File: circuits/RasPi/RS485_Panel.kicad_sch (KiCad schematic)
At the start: 43 parts, among them J8 Conn_01x07_MountingPin, Q18 S8550, Q19 S8550, Q20 S8550, Q3 S8550, Q4 S8550, Q5 S8550, U10 MAX3485, U11 MAX3485, U12 MAX3485, U13 MAX3485, U8 MAX3485, U9 MAX3485

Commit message: PDFプロット
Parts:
- removed C37: 0.1uF, Capacitor_SMD:C_0402_1005Metric, symbol Device:C
- removed Q20: S8550, Package_TO_SOT_SMD:SOT-23, symbol Device:Q_PNP_BEC
- removed R88, R93, R94: 2.2k, Resistor_SMD:R_0402_1005Metric, symbol Device:R
- removed R91: 7.5k, Resistor_SMD:R_0603_1608Metric, symbol Device:R
- removed R92: 20k, Resistor_SMD:R_0402_1005Metric, symbol Device:R
- removed U13: MAX3485, Package_SO:SOP-8_3.9x4.9mm_P1.27mm, symbol Interface_UART:MAX3485
- added C14: 0.1uF, Capacitor_SMD:C_0402_1005Metric, symbol Device:C
- added Q2: S8550, Package_TO_SOT_SMD:SOT-23, symbol Device:Q_PNP_BEC
- added R24, R28: 7.5k, Resistor_SMD:R_0603_1608Metric, symbol Device:R
- added R25: 20k, Resistor_SMD:R_0402_1005Metric, symbol Device:R
- added R26, R27: 2.2k, Resistor_SMD:R_0402_1005Metric, symbol Device:R
- added U5: MAX3485, Package_SO:SOP-8_3.9x4.9mm_P1.27mm, symbol Interface_UART:MAX3485
- J8: footprint (none) -> Connector_Molex:Molex_PicoBlade_53261-0771_1x07-1MP_P1.25mm_Horizontal
- R34, R38, R74, R78: value 7.5k -> 20k; footprint Resistor_SMD:R_0603_1608Metric -> Resistor_SMD:R_0402_1005Metric
- R35, R39, R75, R79: value 20k -> 2.2k
- R37, R41, R77: value 2.2k -> 7.5k; footprint Resistor_SMD:R_0402_1005Metric -> Resistor_SMD:R_0603_1608Metric
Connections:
- net +3.3V: now also R35.1, R75.1, R79.1, C14.1, Q2.2 (E), R26.1, U5.8 (VCC); no longer C33.1, Q5.2 (E), R36.1, R40.1, R76.1, R87.1, U10.8 (VCC)
- net GNDD: now also R34.2, R36.2, R38.2, R40.2, R74.2, R76.2, R78.2, R87.2, C14.2, R25.2, R27.2, U5.5 (GND); no longer R35.2, R37.2, R39.2, R41.2, R75.2, R77.2, R79.2
- net RS485_Panel0: now also U5.6 (A)
- net at R34.1: now also Q4.3 (C), U9.2 (~{RE}), U9.3 (DE); no longer Q4.1 (B)
- net FPGARX_Panel3TX: now reaches U10.1 (RO)
- net at Q5.3 (C), U10.2 (~{RE}), U10.3 (DE): now also R38.1; no longer R39.1
- net FPGARX_Panel2TX: now reaches U9.1 (RO)
- net at Q18.3 (C): now also R74.1, U11.2 (~{RE}), U11.3 (DE)
- net at U12.7 (B): now also R79.2, R87.1; no longer R87.2
- net at Q18.1 (B): now also R41.1
- net at R78.1: now also Q19.3 (C), U12.2 (~{RE}), U12.3 (DE)
- net FPGARX_Panel5TX: now reaches U12.1 (RO)
- net at Q5.1 (B): now also R37.1; no longer R38.1
- net FPGARX_Panel4TX: now reaches U11.1 (RO)
- net at Q19.1 (B): now also R77.1; no longer R74.1
- net FPGARX_Panel1TX: now reaches U8.1 (RO)
- net Panel1 renamed FPGATX_Panel1RX
- net Panel2 renamed FPGATX_Panel2RX
- net FPGATX_Panel2RX: now also R28.2; no longer R34.2
- net Panel3 renamed FPGATX_Panel3RX
- net FPGATX_Panel3RX: now also R37.2; no longer R38.2
- net Panel4 renamed FPGATX_Panel4RX
- net FPGATX_Panel4RX: now also R41.2; no longer R74.2
- net Panel5 renamed FPGATX_Panel5RX
- net FPGATX_Panel5RX: now also R77.2; no longer R78.2
- new net: R35.2, R36.1, U9.7 (B)
- new net: Q2.1 (B), R24.1
- new net: R39.2, R40.1, U10.7 (B)
- new net: R75.2, R76.1, U11.7 (B)
- new net: C33.1, Q5.2 (E), R39.1, U10.8 (VCC)
- new net: R26.2, R27.1, U5.7 (B)
- new net: Q4.1 (B), R28.1
- new net: Q2.3 (C), R25.1, U5.2 (~{RE}), U5.3 (DE)
- new net FPGARX_Panel0TX: U5.1 (RO)
- new net FPGATX_Panel0RX: R24.2, U5.4 (DI)
- no-connect marks 6 -> 0
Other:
- moved on the sheet: C28, J8, Q3, R30, R31, R32, R33, U8

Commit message: panelフットプリント配置
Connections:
- net +3.3V: now also C33.1, Q5.2 (E), R39.1, U10.8 (VCC)
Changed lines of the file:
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@@
     )
   )
-  (symbol (lib_id "power:+3.3V") (at 132.08 99.06 0) (unit 1)
+  (symbol (lib_id "power:+3.3V") (at 137.16 101.6 0) (unit 1)
     (in_bom yes) (on_board yes) (dnp no)
-    (property "Reference" "#PWR050" (at 132.08 102.87 0)
+    (property "Reference" "#PWR050" (at 137.16 105.41 0)
       (effects (font (size 1.27 1.27)) hide)
     )
-    (property "Value" "+3.3V" (at 131.445 94.615 0)
+    (property "Value" "+3.3V" (at 136.525 97.155 0)
       (effects (font (size 1.27 1.27)))
     )
-    (property "Footprint" "" (at 132.08 99.06 0)
+    (property "Footprint" "" (at 137.16 101.6 0)
       (effects (font (size 1.27 1.27)) hide)
     )
-    (property "Datasheet" "" (at 132.08 99.06 0)
+    (property "Datasheet" "" (at 137.16 101.6 0)
       (effects (font (size 1.27 1.27)) hide)
     )

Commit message: raspi基板回路図
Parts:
- removed J8: Conn_01x07_MountingPin, Connector_Molex:Molex_PicoBlade_53261-0771_1x07-1MP_P1.25mm_Horizontal, symbol Connector_Generic_MountingPin:Conn_01x07_MountingPin
- added J15: Conn_01x08_MountingPin, Connector_Molex:Molex_PicoBlade_53261-0871_1x08-1MP_P1.25mm_Horizontal, symbol Connector_Generic_MountingPin:Conn_01x08_MountingPin
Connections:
- net GNDD: now also J15.1 (Pin_1), J15.MP (MountPin)
- net RS485_Panel0: now also J15.2 (Pin_2)
- net RS485_Panel1: now also J15.3 (Pin_3)
- net RS485_Panel2: now also J15.4 (Pin_4)
- net RS485_Panel3: now also J15.5 (Pin_5)
- net RS485_Panel4: now also J15.6 (Pin_6)
- net RS485_Panel5: now also J15.7 (Pin_7)
- new net Panel_PWRCtrl: J15.8 (Pin_8)
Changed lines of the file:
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@@
+    (stroke (width 0) (type default))
+  )
+  (wire (pts (xy 264.16 96.52) (xy 269.24 96.52))
     (stroke (width 0) (type default))
   )
@@
     (stroke (width 0) (type default))
   )
-  (wire (pts (xy 274.32 99.06) (xy 274.32 101.6))
+  (wire (pts (xy 274.32 101.6) (xy 274.32 104.14))
     (stroke (width 0) (type default))
   )
@@
     (effects (font (size 1.27 1.27)) (justify right))
   )
+  (hierarchical_label "Panel_PWRCtrl" (shape input) (at 264.16 96.52 180) (fields_autoplaced)
+    (effects (font (size 1.27 1.27)) (justify right))
+  )
   (hierarchical_label "FPGATX_Panel5RX" (shape input) (at 190.5 127 180) (fields_autoplaced)
     (effects (font (size 1.27 1.27)) (justify right))
@@
         (path "/689a9e74-f202-4ea4-bfbb-4341f2549250/a0e6e20f-c732-4650-b515-927ea2aa6bd5/3bc4b57b-efe0-4a5f-af76-0ef1a38dbbd4"
           (reference "R35") (unit 1)
+        )
+      )
+    )
+  )
+  (symbol (lib_id "Connector_Generic_MountingPin:Conn_01x08_MountingPin") (at 274.32 86.36 0) (unit 1)
+    (in_bom yes) (on_board yes) (dnp no) (fields_autoplaced)
+    (property "Reference" "J15" (at 276.86 86.7156 0)
+      (effects (font (size 1.27 1.27)) (justify left))
+    )
+    (property "Value" "Conn_01x08_MountingPin" (at 276.86 89.2556 0)
+      (effects (font (size 1.27 1.27)) (justify left))
+    )
+    (property "Footprint" "Connector_Molex:Molex_PicoBlade_53261-0871_1x08-1MP_P1.25mm_Horizontal" (at 274.32 86.36 0)
+      (effects (font (size 1.27 1.27)) hide)
+    )
+    (property "Datasheet" "~" (at 274.32 86.36 0)
+      (effects (font (size 1.27 1.27)) hide)
+    )
+    (pin "8")
+    (pin "MP")
+    (pin "1")
+    (pin "4")
+    (pin "5")
+    (pin "2")
+    (pin "3")
+    (pin "6")
+    (pin "7")
+    (instances
+      (project "RasPi"
+        (path "/689a9e74-f202-4ea4-bfbb-4341f2549250/a0e6e20f-c732-4650-b515-927ea2aa6bd5/3bc4b57b-efe0-4a5f-af76-0ef1a38dbbd4"
+          (reference "J15") (unit 1)
         )
       )
@@
     )
   )
-  (symbol (lib_id "power:GNDD") (at 274.32 101.6 0) (unit 1)
-    (in_bom yes) (on_board yes) (dnp no)
-    (property "Reference" "#PWR077" (at 274.32 107.95 0)
-      (effects (font (size 1.27 1.27)) hide)
-    )
-    (property "Value" "GNDD" (at 274.32 105.41 0)
-      (effects (font (size 1.27 1.27)))
-    )
-    (property "Footprint" "" (at 274.32 101.6 0)
-      (effects (font (size 1.27 1.27)) hide)
-    )
-    (property "Datasheet" "" (at 274.32 101.6 0)
+  (symbol (lib_id "power:GNDD") (at 274.32 104.14 0) (unit 1)
+    (in_bom yes) (on_board yes) (dnp no)
+    (property "Reference" "#PWR077" (at 274.32 110.49 0)
+      (effects (font (size 1.27 1.27)) hide)
+    )
+    (property "Value" "GNDD" (at 274.32 107.95 0)
+      (effects (font (size 1.27 1.27)))
+    )
+    (property "Footprint" "" (at 274.32 104.14 0)
+      (effects (font (size 1.27 1.27)) hide)
+    )
+    (property "Datasheet" "" (at 274.32 104.14 0)
       (effects (font (size 1.27 1.27)) hide)
     )
@@
         )
       )
-    )
-  )
-  (symbol (lib_id "Connector_Generic_MountingPin:Conn_01x07_MountingPin") (at 274.32 86.36 0) (unit 1)
-    (in_bom yes) (on_board yes) (dnp no)
-    (property "Reference" "J8" (at 251.46 106.68 0)
-      (effects (font (size 1.27 1.27)) (justify left))
-    )
-    (property "Value" "Conn_01x07_MountingPin" (at 251.46 109.22 0)
-      (effects (font (size 1.27 1.27)) (justify left))
-    )
-    (property "Footprint" "Connector_Molex:Molex_PicoBlade_53261-0771_1x07-1MP_P1.25mm_Horizontal" (at 274.32 86.36 0)
-      (effects (font (size 1.27 1.27)) hide)
-    )
-    (property "Datasheet" "~" (at 274.32 86.36 0)
-      (effects (font (size 1.27 1.27)) hide)
-    )
-    (pin "2")
-    (pin "3")
-    (pin "1")
-    (pin "7")
-    (pin "4")
-    (pin "5")
-    (pin "MP")
-    (pin "6")
-    (instances
-      (project "RasPi"
-        (path "/689a9e74-f202-4ea4-bfbb-4341f2549250/a0e6e20f-c732-4650-b515-927ea2aa6bd5/3bc4b57b-efe0-4a5f-af76-0ef1a38dbbd4"
-          (reference "J8") (unit 1)
-        )
-      )

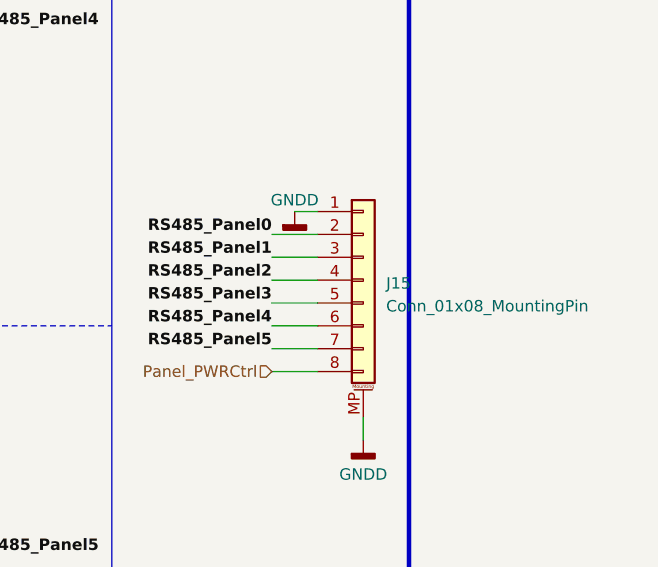
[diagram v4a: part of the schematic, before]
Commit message: 発注第2弾
RasPi発注
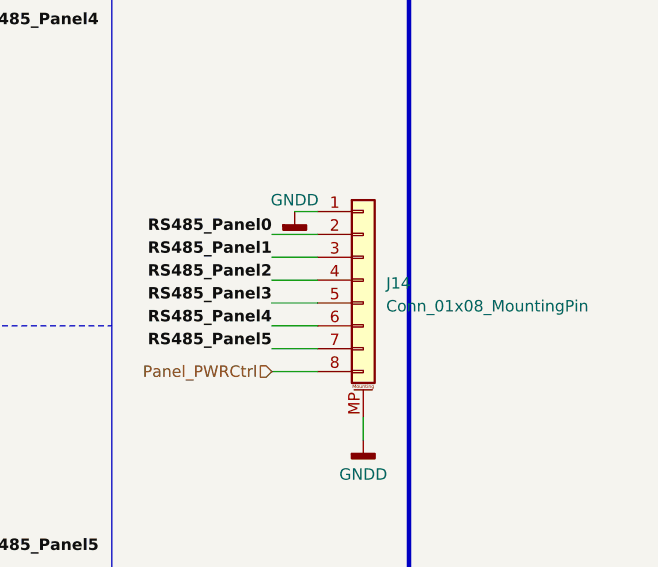
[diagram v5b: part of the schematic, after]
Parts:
- Q18, Q2, Q3, Q4, Q5: footprint Package_TO_SOT_SMD:SOT-23 -> Package_TO_SOT_SMD:SC-59
- renumbered J15 to J14
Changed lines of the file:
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@@
   (symbol (lib_id "Connector_Generic_MountingPin:Conn_01x08_MountingPin") (at 274.32 86.36 0) (unit 1)
     (in_bom yes) (on_board yes) (dnp no) (fields_autoplaced)
-    (property "Reference" "J15" (at 276.86 86.7156 0)
+    (property "Reference" "J14" (at 276.86 86.7156 0)
       (effects (font (size 1.27 1.27)) (justify left))
     )
@@
       (project "RasPi"
         (path "/689a9e74-f202-4ea4-bfbb-4341f2549250/a0e6e20f-c732-4650-b515-927ea2aa6bd5/3bc4b57b-efe0-4a5f-af76-0ef1a38dbbd4"
-          (reference "J15") (unit 1)
+          (reference "J14") (unit 1)
         )
       )
@@
       (effects (font (size 1.27 1.27)) (justify left))
     )
-    (property "Footprint" "Package_TO_SOT_SMD:SOT-23" (at 203.2 53.34 0)
+    (property "Footprint" "Package_TO_SOT_SMD:SC-59" (at 203.2 53.34 0)
       (effects (font (size 1.27 1.27)) hide)
     )
@@
       (effects (font (size 1.27 1.27)) (justify left))
     )
-    (property "Footprint" "Package_TO_SOT_SMD:SOT-23" (at 127 53.34 0)
+    (property "Footprint" "Package_TO_SOT_SMD:SC-59" (at 127 53.34 0)
       (effects (font (size 1.27 1.27)) hide)
     )
@@
       (effects (font (size 1.27 1.27)) (justify left))
     )
-    (property "Footprint" "Package_TO_SOT_SMD:SOT-23" (at 50.8 53.34 0)
+    (property "Footprint" "Package_TO_SOT_SMD:SC-59" (at 50.8 53.34 0)
       (effects (font (size 1.27 1.27)) hide)
     )
@@
       (effects (font (size 1.27 1.27)) (justify left))
     )
-    (property "Footprint" "Package_TO_SOT_SMD:SOT-23" (at 127 111.76 0)
+    (property "Footprint" "Package_TO_SOT_SMD:SC-59" (at 127 111.76 0)
       (effects (font (size 1.27 1.27)) hide)
     )
@@
       (effects (font (size 1.27 1.27)) (justify left))
     )
-    (property "Footprint" "Package_TO_SOT_SMD:SOT-23" (at 50.8 111.76 0)
-      (effects (font (size 1.27 1.27)) hide)
-    )
+    (property "Footprint" "Package_TO_SOT_SMD:SC-59" (at 50.8 111.76 0)
+      (effects (font (size 1.27 1.27)) hide)
+    )

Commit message: 発注第3弾
DCDC、MD追加
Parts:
- removed U10, U11, U12, U5, U8, U9: MAX3485, Package_SO:SOP-8_3.9x4.9mm_P1.27mm, symbol Interface_UART:MAX3485
- added U10, U11, U20, U5, U8, U9: MAX485E, Package_SO:SOP-8_3.9x4.9mm_P1.27mm, symbol Interface_UART:MAX485E
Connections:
- net +3.3V: now also U10.8 (VCC), U11.8 (VCC), U20.8 (VCC), U5.8 (VCC), U8.8 (VCC), U9.8 (VCC)
- net FPGARX_Panel0TX: now also U5.1 (RO)
- net FPGARX_Panel1TX: now also U8.1 (RO)
- net FPGARX_Panel2TX: now also U9.1 (RO)
- net FPGARX_Panel3TX: now also U10.1 (RO)
- net FPGARX_Panel4TX: now also U20.1 (RO)
- net FPGARX_Panel5TX: now also U11.1 (RO)
- net FPGATX_Panel0RX: now also U5.4 (DI)
- net FPGATX_Panel1RX: now also U8.4 (DI)
- net FPGATX_Panel2RX: now also U9.4 (DI)
- net FPGATX_Panel3RX: now also U10.4 (DI)
- net FPGATX_Panel4RX: now also U20.4 (DI)
- net FPGATX_Panel5RX: now also U11.4 (DI)
- net GNDD: now also U10.5 (GND), U11.5 (GND), U20.5 (GND), U5.5 (GND), U8.5 (GND), U9.5 (GND)
- net RS485_Panel0: now also U5.6 (A)
- net RS485_Panel1: now also U8.6 (A)
- net RS485_Panel2: now also U9.6 (A)
- net RS485_Panel3: now also U10.6 (A)
- net RS485_Panel4: now also U20.6 (A)
- net RS485_Panel5: now also U11.6 (A)
- net at R35.2, R36.1: now also U9.7 (B)
- net at Q18.3 (C), R74.1: now also U20.2 (~{RE}), U20.3 (DE)
- net at R39.2, R40.1: now also U10.7 (B)
- net at Q5.3 (C), R38.1: now also U10.2 (~{RE}), U10.3 (DE)
- net at R26.2, R27.1: now also U5.7 (B)
- net at Q19.3 (C), R78.1: now also U11.2 (~{RE}), U11.3 (DE)
- net at R75.2, R76.1: now also U20.7 (B)
- net at Q3.3 (C), R31.1: now also U8.2 (~{RE}), U8.3 (DE)
- net at R32.2, R33.1: now also U8.7 (B)
- net at Q4.3 (C), R34.1: now also U9.2 (~{RE}), U9.3 (DE)
- net at Q2.3 (C), R25.1: now also U5.2 (~{RE}), U5.3 (DE)
- net at R79.2, R87.1: now also U11.7 (B)
